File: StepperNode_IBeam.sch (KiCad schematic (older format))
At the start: 1 part

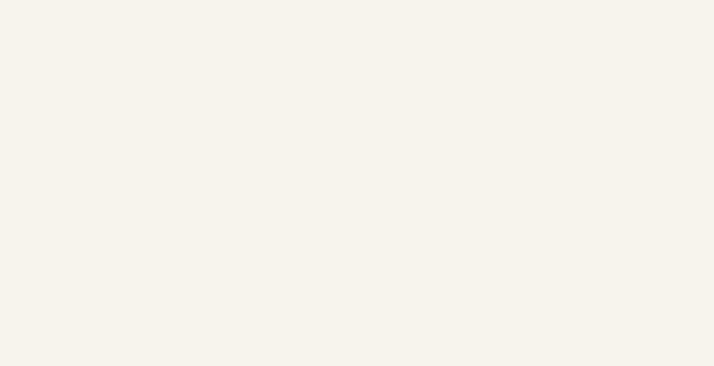
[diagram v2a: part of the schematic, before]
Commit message: Remove Gimbal Functions
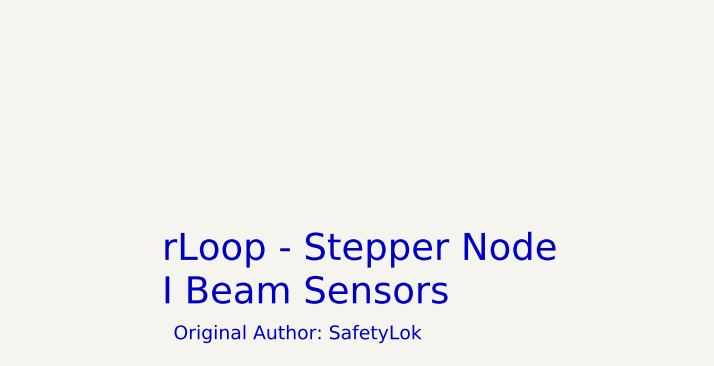
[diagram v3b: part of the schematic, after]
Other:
- note added: "Original Author: SafetyLok"
- note added: "rLoop - Stepper Node\nI Beam Sensors\n"
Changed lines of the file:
@@
 $Descr A3 16535 11693
 encoding utf-8
-Sheet 15 17
+Sheet 14 15
 Title "I Beam Laterial (Yaw) Sensors"
 Date ""
@@
 Text HLabel 9250 3400 2    60   Input ~ 0
 CHB_SPI_SCK
+Text Notes 11900 10350 0    118  ~ 0
+rLoop - Stepper Node\nI Beam Sensors\n
+Text Notes 11950 10500 0    60   ~ 0
+Original Author: SafetyLok
 $EndSCHEMATC

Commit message: First Revision -
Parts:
- removed U?: MAX3140, symbol MAX3140
- added C26, C27, C28: C_100nF_50V, RLOOP_FOOTPRINTS:rLoop_C_0603, symbol C_100nF_50V
- added P7, P8, P9: TE_640456-8, RLOOP_FOOTPRINTS:rLoop_TE640456-8, symbol TE_640456-8
- added R11, R12, R13: 2.2K, RLOOP_FOOTPRINTS:rLoop_R_0603, symbol 2.2K
- added U16, U17, U18: DS8921AMX, RLOOP_FOOTPRINTS:rLoop_SOIC8, symbol DS8921AMX
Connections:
- net labels added: +24V_A, +5V_A, GNDD, IB_FL_RX_3V, IB_FL_TX, IB_FR_RX_3V, IB_FR_TX, IB_RL_RX_3V, IB_RL_TX
- net labels removed: CHA_IB_FL_NCS, CHA_IB_FL_NIRQ, CHA_IB_FR_NCS, CHA_IB_FR_NIRQ, CHA_IB_RL_NCS, CHA_IB_RL_NIRQ, CHA_SPI_MISO, CHA_SPI_MOSI, CHA_SPI_SCK, CHB_IB_FL_NCS, CHB_IB_FL_NIRQ, CHB_IB_FR_NCS, CHB_IB_FR_NIRQ, CHB_IB_RL_NCS, CHB_IB_RL_NIRQ, CHB_SPI_MISO, CHB_SPI_MOSI, CHB_SPI_SCK
- wire segments 5 -> 45
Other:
- note added: "IBeam Front Left"
- note added: "IBeam Front Right"
- note added: "IBeam Rear Left"
- note added: "Resistor for 3.3V conversion"

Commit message: Update per design review.
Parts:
- added R? (x6): 100R, RLOOP_FOOTPRINTS:rLoop_R_0603, symbol 100R
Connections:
- net at P8.1 (P1), U17.8 (RI+): now also R?.2
- net at P8.2 (P2), U17.7 (RI-): now also R?.1
- net at P8.3 (P3), U17.6 (DO+): now also R?.2
- net at P8.4 (P4), U17.5 (DO-): now also R?.1
- net at P9.1 (P1), U18.8 (RI+): now also R?.2
- net at P9.2 (P2), U18.7 (RI-): now also R?.1
- net at P9.3 (P3), U18.6 (DO+): now also R?.2
- net at P9.4 (P4), U18.5 (DO-): now also R?.1
- net at P7.1 (P1), U16.8 (RI+): now also R?.2
- net at P7.2 (P2), U16.7 (RI-): now also R?.1
- net at P7.3 (P3), U16.6 (DO+): now also R?.2
- net at P7.4 (P4), U16.5 (DO-): now also R?.1
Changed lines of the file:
@@
 Title "I Beam Laterial (Yaw) Sensors"
 Date ""
-Rev "1"
+Rev "2"
 Comp ""
 Comment1 ""
@@
 	1    0    0    -1
 $EndComp
+$Comp
+L 100R R?
+U 1 1 575CFED7
+P 5500 2400
+F 0 "R?" V 5580 2400 50  0000 C CNN
+F 1 "100R" V 5500 2400 50  0000 C CNN
+F 2 "RLOOP_FOOTPRINTS:rLoop_R_0603" V 5430 2400 50  0001 C CNN
+F 3 "" H 5500 2400 50  0000 C CNN
+	1    5500 2400
+	1    0    0    -1
+$EndComp
+$Comp
+L 100R R?
+U 1 1 575CFF32
+P 5800 2400
+F 0 "R?" V 5880 2400 50  0000 C CNN
+F 1 "100R" V 5800 2400 50  0000 C CNN
+F 2 "RLOOP_FOOTPRINTS:rLoop_R_0603" V 5730 2400 50  0001 C CNN
+F 3 "" H 5800 2400 50  0000 C CNN
+	1    5800 2400
+	1    0    0    -1
+$EndComp
+Wire Wire Line
+	5500 2550 5500 2750
+Connection ~ 5500 2750
+Wire Wire Line
+	5500 2250 5600 2250
+Wire Wire Line
+	5600 2250 5600 2850
+Connection ~ 5600 2850
+Wire Wire Line
+	5800 2550 5800 2950
+Connection ~ 5800 2950
+Wire Wire Line
+	5800 2250 5900 2250
+Wire Wire Line
+	5900 2250 5900 3050
+Connection ~ 5900 3050
+$Comp
+L 100R R?
+U 1 1 575D01AA
+P 11750 2500
+F 0 "R?" V 11830 2500 50  0000 C CNN
+F 1 "100R" V 11750 2500 50  0000 C CNN
+F 2 "RLOOP_FOOTPRINTS:rLoop_R_0603" V 11680 2500 50  0001 C CNN
+F 3 "" H 11750 2500 50  0000 C CNN
+	1    11750 2500
+	1    0    0    -1
+$EndComp
+$Comp
+L 100R R?
+U 1 1 575D01B0
+P 12050 2500
+F 0 "R?" V 12130 2500 50  0000 C CNN
+F 1 "100R" V 12050 2500 50  0000 C CNN
+F 2 "RLOOP_FOOTPRINTS:rLoop_R_0603" V 11980 2500 50  0001 C CNN
+F 3 "" H 12050 2500 50  0000 C CNN
+	1    12050 2500
+	1    0    0    -1
+$EndComp
+Wire Wire Line
+	11750 2650 11750 2850
+Connection ~ 11750 2850
+Wire Wire Line
+	11750 2350 11850 2350
+Wire Wire Line
+	11850 2350 11850 2950
+Connection ~ 11850 2950
+Wire Wire Line
+	12050 2650 12050 3050
+Connection ~ 12050 3050
+Wire Wire Line
+	12050 2350 12150 2350
+Wire Wire Line
+	12150 2350 12150 3150
+Connection ~ 12150 3150
+$Comp
+L 100R R?
+U 1 1 575D04D0
+P 11800 5400
+F 0 "R?" V 11880 5400 50  0000 C CNN
+F 1 "100R" V 11800 5400 50  0000 C CNN
+F 2 "RLOOP_FOOTPRINTS:rLoop_R_0603" V 11730 5400 50  0001 C CNN
+F 3 "" H 11800 5400 50  0000 C CNN
+	1    11800 5400
+	1    0    0    -1
+$EndComp
+$Comp
+L 100R R?
+U 1 1 575D04D6
+P 12100 5400
+F 0 "R?" V 12180 5400 50  0000 C CNN
+F 1 "100R" V 12100 5400 50  0000 C CNN
+F 2 "RLOOP_FOOTPRINTS:rLoop_R_0603" V 12030 5400 50  0001 C CNN
+F 3 "" H 12100 5400 50  0000 C CNN
+	1    12100 5400
+	1    0    0    -1
+$EndComp
+Wire Wire Line
+	11800 5550 11800 5750
+Connection ~ 11800 5750
+Wire Wire Line
+	11800 5250 11900 5250
+Wire Wire Line
+	11900 5250 11900 5850
+Connection ~ 11900 5850
+Wire Wire Line
+	12100 5550 12100 5950
+Connection ~ 12100 5950
+Wire Wire Line
+	12100 5250 12200 5250
+Wire Wire Line
+	12200 5250 12200 6050
+Connection ~ 12200 6050
 $EndSCHEMATC

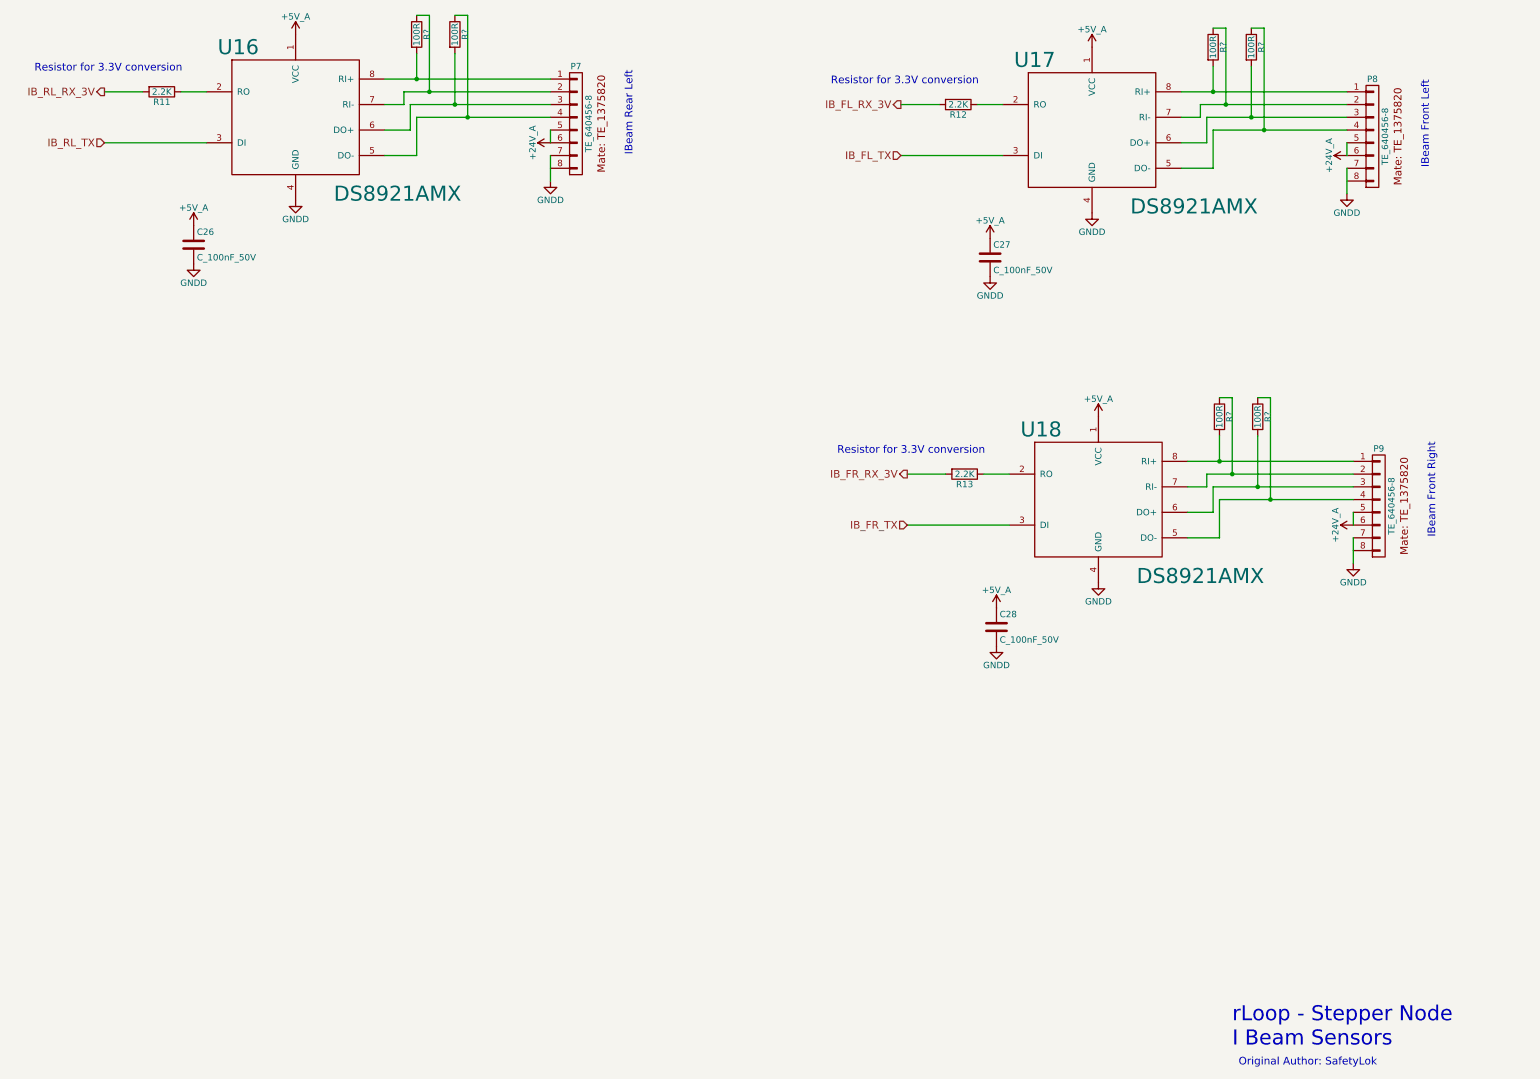
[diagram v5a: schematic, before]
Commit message: Fix most ERC warnings (non-connected pins, etc)
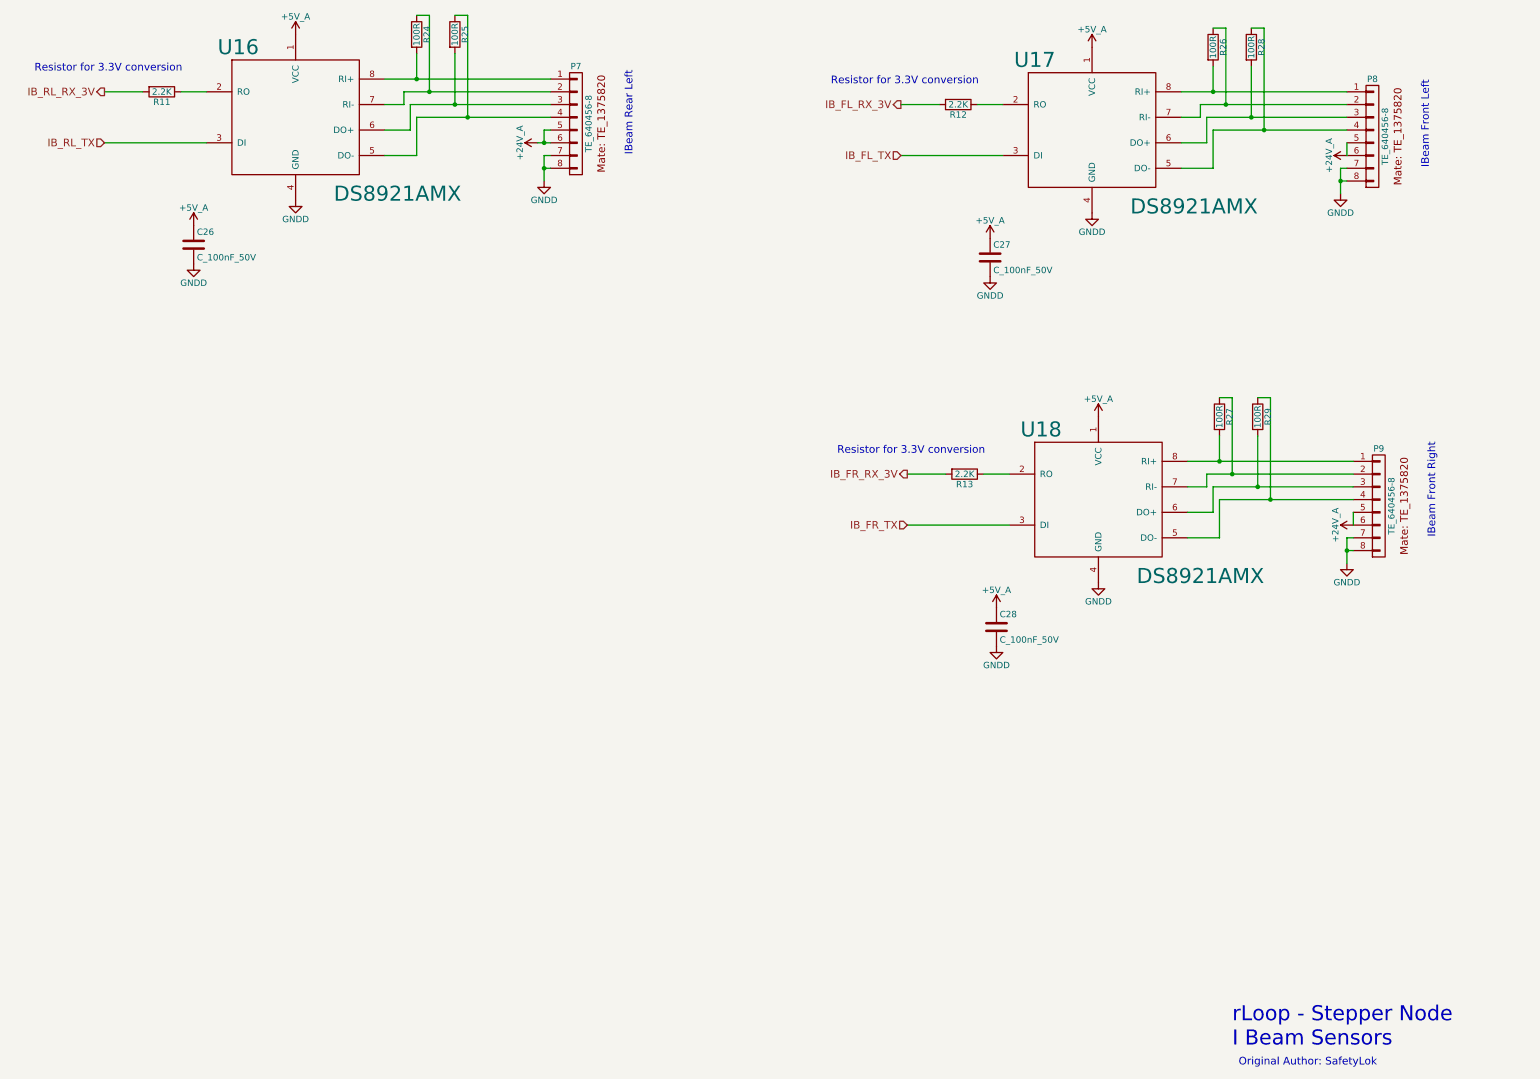
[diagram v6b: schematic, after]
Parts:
- gave numbers to parts that had none: 6
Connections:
- net GNDD: now also P7.8 (P8), P8.8 (P8), P9.8 (P8)
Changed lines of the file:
@@
 Original Author: SafetyLok
 $Comp
-L +5V_A #PWR111
+L +5V_A #PWR0111
 U 1 1 575D6770
 P 10800 2500
-F 0 "#PWR111" H 10800 2350 50  0001 C CNN
+F 0 "#PWR0111" H 10800 2350 50  0001 C CNN
 F 1 "+5V_A" H 10800 2640 50  0000 C CNN
 F 2 "" H 10800 2500 60  0000 C CNN
@@
 $EndComp
 $Comp
-L GNDD #PWR112
+L GNDD #PWR0112
 U 1 1 575D67A2
 P 10800 3800
-F 0 "#PWR112" H 10800 3550 50  0001 C CNN
+F 0 "#PWR0112" H 10800 3550 50  0001 C CNN
 F 1 "GNDD" H 10800 3650 50  0000 C CNN
 F 2 "" H 10800 3800 50  0000 C CNN
@@
 $EndComp
 $Comp
-L GNDD #PWR108
+L GNDD #PWR0113
 U 1 1 575D6A0C
 P 10000 4300
-F 0 "#PWR108" H 10000 4050 50  0001 C CNN
+F 0 "#PWR0113" H 10000 4050 50  0001 C CNN
 F 1 "GNDD" H 10000 4150 50  0000 C CNN
 F 2 "" H 10000 4300 50  0000 C CNN
@@
 $EndComp
 $Comp
-L +5V_A #PWR107
+L +5V_A #PWR0114
 U 1 1 575D6A18
 P 10000 4000
-F 0 "#PWR107" H 10000 3850 50  0001 C CNN
+F 0 "#PWR0114" H 10000 3850 50  0001 C CNN
 F 1 "+5V_A" H 10000 4140 50  0000 C CNN
 F 2 "" H 10000 4000 60  0000 C CNN
@@
 IBeam Front Left
 $Comp
-L +5V_A #PWR113
+L +5V_A #PWR0115
 U 1 1 575D7948
 P 10850 5400
-F 0 "#PWR113" H 10850 5250 50  0001 C CNN
+F 0 "#PWR0115" H 10850 5250 50  0001 C CNN
 F 1 "+5V_A" H 10850 5540 50  0000 C CNN
 F 2 "" H 10850 5400 60  0000 C CNN
@@
 $EndComp
 $Comp
-L GNDD #PWR114
+L GNDD #PWR0116
 U 1 1 575D794E
 P 10850 6700
-F 0 "#PWR114" H 10850 6450 50  0001 C CNN
+F 0 "#PWR0116" H 10850 6450 50  0001 C CNN
 F 1 "GNDD" H 10850 6550 50  0000 C CNN
 F 2 "" H 10850 6700 50  0000 C CNN
@@
 $EndComp
 $Comp
-L GNDD #PWR110
+L GNDD #PWR0117
 U 1 1 575D796A
 P 10050 7200
-F 0 "#PWR110" H 10050 6950 50  0001 C CNN
+F 0 "#PWR0117" H 10050 6950 50  0001 C CNN
 F 1 "GNDD" H 10050 7050 50  0000 C CNN
 F 2 "" H 10050 7200 50  0000 C CNN
@@
 $EndComp
 $Comp
-L +5V_A #PWR109
+L +5V_A #PWR0118
 U 1 1 575D7970
 P 10050 6900
-F 0 "#PWR109" H 10050 6750 50  0001 C CNN
+F 0 "#PWR0118" H 10050 6750 50  0001 C CNN
 F 1 "+5V_A" H 10050 7040 50  0000 C CNN
 F 2 "" H 10050 6900 60  0000 C CNN
@@
 IBeam Front Right
 $Comp
-L +5V_A #PWR103
+L +5V_A #PWR0119
 U 1 1 575D97A4
 P 4550 2400
-F 0 "#PWR103" H 4550 2250 50  0001 C CNN
+F 0 "#PWR0119" H 4550 2250 50  0001 C CNN
 F 1 "+5V_A" H 4550 2540 50  0000 C CNN
 F 2 "" H 4550 2400 60  0000 C CNN
@@
 $EndComp
 $Comp
-L GNDD #PWR104
+L GNDD #PWR0120
 U 1 1 575D97AA
 P 4550 3700
-F 0 "#PWR104" H 4550 3450 50  0001 C CNN
+F 0 "#PWR0120" H 4550 3450 50  0001 C CNN
 F 1 "GNDD" H 4550 3550 50  0000 C CNN
 F 2 "" H 4550 3700 50  0000 C CNN
@@
 $EndComp
 $Comp
-L GNDD #PWR102
+L GNDD #PWR0121
 U 1 1 575D97C6
 P 3750 4200
-F 0 "#PWR102" H 3750 3950 50  0001 C CNN
+F 0 "#PWR0121" H 3750 3950 50  0001 C CNN
 F 1 "GNDD" H 3750 4050 50  0000 C CNN
 F 2 "" H 3750 4200 50  0000 C CNN
@@
 $EndComp
 $Comp
-L +5V_A #PWR101
+L +5V_A #PWR0122
 U 1 1 575D97CC
 P 3750 3900
-F 0 "#PWR101" H 3750 3750 50  0001 C CNN
+F 0 "#PWR0122" H 3750 3750 50  0001 C CNN
 F 1 "+5V_A" H 3750 4040 50  0000 C CNN
 F 2 "" H 3750 3900 60  0000 C CNN
@@
 	11750 3450 11500 3450
 $Comp
-L +24V_A #PWR115
+L +24V_A #PWR0123
 U 1 1 575BC30F
 P 12800 3350
-F 0 "#PWR115" H 12800 3200 50  0001 C CNN
+F 0 "#PWR0123" H 12800 3200 50  0001 C CNN
 F 1 "+24V_A" H 12800 3490 50  0000 C CNN
 F 2 "" H 12800 3350 60  0000 C CNN
@@
 $EndComp
 $Comp
-L GNDD #PWR116
+L GNDD #PWR0124
 U 1 1 575BC33B
-P 12800 3650
-F 0 "#PWR116" H 12800 3400 50  0001 C CNN
-F 1 "GNDD" H 12800 3500 50  0000 C CNN
-F 2 "" H 12800 3650 50  0000 C CNN
-F 3 "" H 12800 3650 50  0000 C CNN
-	1    12800 3650
-	1    0    0    -1
-$EndComp
-Wire Wire Line
-	12800 3450 12800 3650
+P 12750 3650
+F 0 "#PWR0124" H 12750 3400 50  0001 C CNN
+F 1 "GNDD" H 12750 3500 50  0000 C CNN
+F 2 "" H 12750 3650 50  0000 C CNN
+F 3 "" H 12750 3650 50  0000 C CNN
+	1    12750 3650
+	1    0    0    -1
+$EndComp
 Wire Wire Line
 	12800 3250 12800 3350
@@
 	11800 6350 11550 6350
 $Comp
-L +24V_A #PWR117
+L +24V_A #PWR0125
 U 1 1 575BC5A3
 P 12850 6250
-F 0 "#PWR117" H 12850 6100 50  0001 C CNN
+F 0 "#PWR0125" H 12850 6100 50  0001 C CNN
 F 1 "+24V_A" H 12850 6390 50  0000 C CNN
 F 2 "" H 12850 6250 60  0000 C CNN
@@
 	0    -1   -1   0
 $EndComp
-Wire Wire Line
-	12850 6350 12850 6550
 Wire Wire Line
 	12850 6150 12850 6250
@@
 	5500 3350 5250 3350
 $Comp
-L +24V_A #PWR105
-U 1 1 575BCD9D
-P 6550 3250
-F 0 "#PWR105" H 6550 3100 50  0001 C CNN
-F 1 "+24V_A" H 6550 3390 50  0000 C CNN
-F 2 "" H 6550 3250 60  0000 C CNN
-F 3 "" H 6550 3250 60  0000 C CNN
-	1    6550 3250
-	0    -1   -1   0
-$EndComp
-Wire Wire Line
-	6550 3350 6550 3550
-Wire Wire Line
-	6550 3150 6550 3250
-$Comp
-L GNDD #PWR106
+L GNDD #PWR0126
 U 1 1 575BCDB3
-P 6550 3550
-F 0 "#PWR106" H 6550 3300 50  0001 C CNN
-F 1 "GNDD" H 6550 3400 50  0000 C CNN
-F 2 "" H 6550 3550 50  0000 C CNN
-F 3 "" H 6550 3550 50  0000 C CNN
-	1    6550 3550
-	1    0    0    -1
-$EndComp
-$Comp
-L GNDD #PWR118
+P 6500 3550
+F 0 "#PWR0126" H 6500 3300 50  0001 C CNN
+F 1 "GNDD" H 6500 3400 50  0000 C CNN
+F 2 "" H 6500 3550 50  0000 C CNN
+F 3 "" H 6500 3550 50  0000 C CNN
+	1    6500 3550
+	1    0    0    -1
+$EndComp
+$Comp
+L GNDD #PWR0127
 U 1 1 575BCE55
-P 12850 6550
-F 0 "#PWR118" H 12850 6300 50  0001 C CNN
-F 1 "GNDD" H 12850 6400 50  0000 C CNN
-F 2 "" H 12850 6550 50  0000 C CNN
-F 3 "" H 12850 6550 50  0000 C CNN
-	1    12850 6550
-	1    0    0    -1
-$EndComp
-$Comp
-L 100R R?
+P 12800 6550
+F 0 "#PWR0127" H 12800 6300 50  0001 C CNN
+F 1 "GNDD" H 12800 6400 50  0000 C CNN
+F 2 "" H 12800 6550 50  0000 C CNN
+F 3 "" H 12800 6550 50  0000 C CNN
+	1    12800 6550
+	1    0    0    -1
+$EndComp
+$Comp
+L 100R R24
 U 1 1 575CFED7
 P 5500 2400
-F 0 "R?" V 5580 2400 50  0000 C CNN
+F 0 "R24" V 5580 2400 50  0000 C CNN
 F 1 "100R" V 5500 2400 50  0000 C CNN
 F 2 "RLOOP_FOOTPRINTS:rLoop_R_0603" V 5430 2400 50  0001 C CNN
@@
 $EndComp
 $Comp
-L 100R R?
+L 100R R25
 U 1 1 575CFF32
 P 5800 2400
-F 0 "R?" V 5880 2400 50  0000 C CNN
+F 0 "R25" V 5880 2400 50  0000 C CNN
 F 1 "100R" V 5800 2400 50  0000 C CNN
 F 2 "RLOOP_FOOTPRINTS:rLoop_R_0603" V 5730 2400 50  0001 C CNN
@@
 Connection ~ 5900 3050
 $Comp
-L 100R R?
+L 100R R26
 U 1 1 575D01AA
 P 11750 2500
-F 0 "R?" V 11830 2500 50  0000 C CNN
+F 0 "R26" V 11830 2500 50  0000 C CNN
 F 1 "100R" V 11750 2500 50  0000 C CNN
 F 2 "RLOOP_FOOTPRINTS:rLoop_R_0603" V 11680 2500 50  0001 C CNN
@@
 $EndComp
 $Comp
-L 100R R?
+L 100R R28
 U 1 1 575D01B0
 P 12050 2500
-F 0 "R?" V 12130 2500 50  0000 C CNN
+F 0 "R28" V 12130 2500 50  0000 C CNN
 F 1 "100R" V 12050 2500 50  0000 C CNN
 F 2 "RLOOP_FOOTPRINTS:rLoop_R_0603" V 11980 2500 50  0001 C CNN
@@
 Connection ~ 12150 3150
 $Comp
-L 100R R?
+L 100R R27
 U 1 1 575D04D0
 P 11800 5400
-F 0 "R?" V 11880 5400 50  0000 C CNN
+F 0 "R27" V 11880 5400 50  0000 C CNN
 F 1 "100R" V 11800 5400 50  0000 C CNN
 F 2 "RLOOP_FOOTPRINTS:rLoop_R_0603" V 11730 5400 50  0001 C CNN
@@
 $EndComp
 $Comp
-L 100R R?
+L 100R R29
 U 1 1 575D04D6
 P 12100 5400
-F 0 "R?" V 12180 5400 50  0000 C CNN
+F 0 "R29" V 12180 5400 50  0000 C CNN
 F 1 "100R" V 12100 5400 50  0000 C CNN
 F 2 "RLOOP_FOOTPRINTS:rLoop_R_0603" V 12030 5400 50  0001 C CNN
@@
 	12200 5250 12200 6050
 Connection ~ 12200 6050
+Wire Wire Line
+	12800 3450 12750 3450
+Wire Wire Line
+	12750 3450 12750 3650
+Wire Wire Line
+	12800 3550 12750 3550
+Connection ~ 12750 3550
+Wire Wire Line
+	12850 6350 12800 6350
+Wire Wire Line
+	12800 6350 12800 6550
+Wire Wire Line
+	12850 6450 12800 6450
+Connection ~ 12800 6450
+$Comp
+L +24V_A #PWR0128
+U 1 1 5762CA19
+P 6450 3250
+F 0 "#PWR0128" H 6450 3100 50  0001 C CNN
+F 1 "+24V_A" H 6450 3390 50  0000 C CNN
+F 2 "" H 6450 3250 60  0000 C CNN
+F 3 "" H 6450 3250 60  0000 C CNN
+	1    6450 3250
+	0    -1   -1   0
+$EndComp
+Wire Wire Line
+	6450 3250 6550 3250
+Wire Wire Line
+	6550 3150 6500 3150
+Wire Wire Line
+	6500 3150 6500 3250
+Connection ~ 6500 3250
+Wire Wire Line
+	6500 3550 6500 3350
+Wire Wire Line
+	6500 3350 6550 3350
+Wire Wire Line
+	6550 3450 6500 3450
+Connection ~ 6500 3450
 $EndSCHEMATC
